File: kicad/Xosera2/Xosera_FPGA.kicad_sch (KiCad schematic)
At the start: 99 parts, among them J1 47589-0001, U1 93LC56BT-I/OT, U2 ICE40UP5K-SG48ITR, U3 FT232H, U4 SG-210STF 12.0000ML3, U5 W25Q32JVSSIM, U6 AP2127K-3.3, U7 AP2127K-1.2, U8 SN74AUP2G125DCUR

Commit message: Make a start on placement
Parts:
- removed H1, H2, H3, H4: MountingHole, vs:MountingHole_2.5mm_M3, symbol UPduino_v3.0:Mechanical_MountingHole
- J1: footprint vs:USB_Micro_AB_Female_0475890001 -> Connector_USB:USB_Micro-AB_Molex_47590-0001
- SJ19, SJ24, SJ25, SJ26: footprint vs:SolderJumper-2_0603_Open_TrianglePad1.0x1.5mm -> Jumper:SolderJumper-2_P1.3mm_Open_RoundedPad1.0x1.5mm
- SJ20, SJ31, SJ34, SJ35, SJ36: footprint vs:ShortedJumper-2_P1.3mm_Bridged_Pad1.0x1.0mm -> Jumper:SolderJumper-2_P1.3mm_Bridged2Bar_RoundedPad1.0x1.5mm
- U1: footprint vs:SOT-23-6 -> Package_TO_SOT_SMD:SOT-23-6
- U3: footprint vs:QFN-48-1EP_8x8mm_P0.5mm_EP6.2x6.2mm -> Package_DFN_QFN:QFN-48-1EP_8x8mm_P0.5mm_EP6.2x6.2mm
- U4: footprint vs:Oscillator_SMD_Abracon_ASDMB-4Pin_2.5x2.0mm -> Oscillator:Oscillator_SMD_Abracon_ASDMB-4Pin_2.5x2.0mm
- U6, U7: footprint vs:SOT-23-5 -> Package_TO_SOT_SMD:SOT-23-5

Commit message: Replace all GALs with one 1504
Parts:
- C10, C12, C13, C14, C15, C16, C18, C2, C25, C3, C36, C4, C5, C6, C7, C8, C9: value 0.1u -> 100n; footprint Capacitor_SMD:C_0603_1608Metric -> Capacitor_SMD:C_0402_1005Metric
- C17: value 0.1u -> 100m; footprint Capacitor_SMD:C_0603_1608Metric -> Capacitor_SMD:C_0402_1005Metric
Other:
- title: Xosera rosco_m68k daughterboard -> rosco_m68k Super Board
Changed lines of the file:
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@@
   (paper "A3")
   (title_block
-    (title "Xosera rosco_m68k daughterboard")
-    (date "2024-02-08")
+    (title "rosco_m68k Super Board")
+    (date "2024-02-11")
     (rev "0")
     (company "The Really Old-School Company Limited & XarkLabs")
     (comment 1 "Copyright (c)2023")
     (comment 2 "CERN OHL & MIT License")
+    (comment 3 "Featuring Xosera & MarkM's IDE")
   )
   (junction (at 262.89 208.28) (diameter 0) (color 0 0 0 0)
@@
       (effects (font (size 1.27 1.27)) (justify left))
     )
-    (property "Value" "0.1u" (at 141.351 181.483 0)
+    (property "Value" "100n" (at 141.351 181.483 0)
       (effects (font (size 1.27 1.27)) (justify left))
     )
-    (property "Footprint" "Capacitor_SMD:C_0603_1608Metric" (at 139.3952 184.15 0)
+    (property "Footprint" "Capacitor_SMD:C_0402_1005Metric" (at 139.3952 184.15 0)
       (effects (font (size 1.27 1.27)) hide)
     )
@@
       (effects (font (size 1.27 1.27)) (justify left))
     )
-    (property "Value" "0.1u" (at 121.031 181.483 0)
+    (property "Value" "100n" (at 121.031 181.483 0)
       (effects (font (size 1.27 1.27)) (justify left))
     )
-    (property "Footprint" "Capacitor_SMD:C_0603_1608Metric" (at 119.0752 184.15 0)
+    (property "Footprint" "Capacitor_SMD:C_0402_1005Metric" (at 119.0752 184.15 0)
       (effects (font (size 1.27 1.27)) hide)
     )
@@
       (effects (font (size 1.27 1.27)) (justify left))
     )
-    (property "Value" "0.1u" (at 43.561 195.453 0)
+    (property "Value" "100n" (at 43.561 195.453 0)
       (effects (font (size 1.27 1.27)) (justify left))
     )
-    (property "Footprint" "Capacitor_SMD:C_0603_1608Metric" (at 41.6052 198.12 0)
+    (property "Footprint" "Capacitor_SMD:C_0402_1005Metric" (at 41.6052 198.12 0)
       (effects (font (size 1.27 1.27)) hide)
     )
@@
       (effects (font (size 1.27 1.27)) (justify left))
     )
-    (property "Value" "0.1u" (at 61.341 181.483 0)
+    (property "Value" "100n" (at 61.341 181.483 0)
       (effects (font (size 1.27 1.27)) (justify left))
     )
-    (property "Footprint" "Capacitor_SMD:C_0603_1608Metric" (at 59.3852 184.15 0)
+    (property "Footprint" "Capacitor_SMD:C_0402_1005Metric" (at 59.3852 184.15 0)
       (effects (font (size 1.27 1.27)) hide)
     )
@@
       (effects (font (size 1.27 1.27)) (justify left))
     )
-    (property "Value" "0.1u" (at 62.611 104.013 0)
+    (property "Value" "100n" (at 62.611 104.013 0)
       (effects (font (size 1.27 1.27)) (justify left))
     )
-    (property "Footprint" "Capacitor_SMD:C_0603_1608Metric" (at 60.6552 106.68 0)
+    (property "Footprint" "Capacitor_SMD:C_0402_1005Metric" (at 60.6552 106.68 0)
       (effects (font (size 1.27 1.27)) hide)
     )
@@
       (effects (font (size 1.27 1.27)) (justify left))
     )
-    (property "Value" "0.1u" (at 53.721 50.673 0)
+    (property "Value" "100n" (at 53.721 50.673 0)
       (effects (font (size 1.27 1.27)) (justify left))
     )
-    (property "Footprint" "Capacitor_SMD:C_0603_1608Metric" (at 51.7652 53.34 0)
+    (property "Footprint" "Capacitor_SMD:C_0402_1005Metric" (at 51.7652 53.34 0)
       (effects (font (size 1.27 1.27)) hide)
     )
@@
       (effects (font (size 1.27 1.27)) (justify left))
     )
-    (property "Value" "0.1u" (at 376.301 74.803 0)
+    (property "Value" "100n" (at 376.301 74.803 0)
       (effects (font (size 1.27 1.27)) (justify left))
     )
-    (property "Footprint" "Capacitor_SMD:C_0603_1608Metric" (at 374.3452 77.47 0)
+    (property "Footprint" "Capacitor_SMD:C_0402_1005Metric" (at 374.3452 77.47 0)
       (effects (font (size 1.27 1.27)) hide)
     )
@@
       (effects (font (size 1.27 1.27)))
     )
-    (property "Value" "0.1u" (at 74.93 207.01 90)
+    (property "Value" "100n" (at 74.93 207.01 90)
       (effects (font (size 1.27 1.27)))
     )
-    (property "Footprint" "Capacitor_SMD:C_0603_1608Metric" (at 71.12 203.2 0)
+    (property "Footprint" "Capacitor_SMD:C_0402_1005Metric" (at 71.12 203.2 0)
       (effects (font (size 1.27 1.27)) hide)
     )
@@
       (effects (font (size 1.27 1.27)) (justify left))
     )
-    (property "Value" "0.1u" (at 165.481 172.593 0)
+    (property "Value" "100n" (at 165.481 172.593 0)
       (effects (font (size 1.27 1.27)) (justify left))
     )
-    (property "Footprint" "Capacitor_SMD:C_0603_1608Metric" (at 163.5252 175.26 0)
+    (property "Footprint" "Capacitor_SMD:C_0402_1005Metric" (at 163.5252 175.26 0)
       (effects (font (size 1.27 1.27)) hide)
     )
@@
       (effects (font (size 1.27 1.27)) (justify left))
     )
-    (property "Value" "0.1u" (at 215.011 82.423 0)
+    (property "Value" "100n" (at 215.011 82.423 0)
       (effects (font (size 1.27 1.27)) (justify left))
     )
-    (property "Footprint" "Capacitor_SMD:C_0603_1608Metric" (at 213.0552 85.09 0)
+    (property "Footprint" "Capacitor_SMD:C_0402_1005Metric" (at 213.0552 85.09 0)
       (effects (font (size 1.27 1.27)) hide)
     )
@@
       (effects (font (size 1.27 1.27)) (justify left))
     )
-    (property "Value" "0.1u" (at 131.191 181.483 0)
+    (property "Value" "100n" (at 131.191 181.483 0)
       (effects (font (size 1.27 1.27)) (justify left))
     )
-    (property "Footprint" "Capacitor_SMD:C_0603_1608Metric" (at 129.2352 184.15 0)
+    (property "Footprint" "Capacitor_SMD:C_0402_1005Metric" (at 129.2352 184.15 0)
       (effects (font (size 1.27 1.27)) hide)
     )
@@
       (effects (font (size 1.27 1.27)) (justify left))
     )
-    (property "Value" "0.1u" (at 310.261 39.243 0)
+    (property "Value" "100n" (at 310.261 39.243 0)
       (effects (font (size 1.27 1.27)) (justify left))
     )
-    (property "Footprint" "Capacitor_SMD:C_0603_1608Metric" (at 308.3052 41.91 0)
+    (property "Footprint" "Capacitor_SMD:C_0402_1005Metric" (at 308.3052 41.91 0)
       (effects (font (size 1.27 1.27)) hide)
     )
@@
       (effects (font (size 1.27 1.27)) (justify left))
     )
-    (property "Value" "0.1u" (at 281.051 83.693 0)
+    (property "Value" "100n" (at 281.051 83.693 0)
       (effects (font (size 1.27 1.27)) (justify left))
     )
-    (property "Footprint" "Capacitor_SMD:C_0603_1608Metric" (at 279.0952 86.36 0)
+    (property "Footprint" "Capacitor_SMD:C_0402_1005Metric" (at 279.0952 86.36 0)
       (effects (font (size 1.27 1.27)) hide)
     )
@@
       (effects (font (size 1.27 1.27)) (justify left))
     )
-    (property "Value" "0.1u" (at 27.051 267.843 0)
+    (property "Value" "100n" (at 27.051 267.843 0)
       (effects (font (size 1.27 1.27)) (justify left))
     )
-    (property "Footprint" "Capacitor_SMD:C_0603_1608Metric" (at 25.0952 270.51 0)
+    (property "Footprint" "Capacitor_SMD:C_0402_1005Metric" (at 25.0952 270.51 0)
       (effects (font (size 1.27 1.27)) hide)
     )
@@
       (effects (font (size 1.27 1.27)) (justify left))
     )
-    (property "Value" "0.1u" (at 164.211 83.693 0)
+    (property "Value" "100n" (at 164.211 83.693 0)
       (effects (font (size 1.27 1.27)) (justify left))
     )
-    (property "Footprint" "Capacitor_SMD:C_0603_1608Metric" (at 162.2552 86.36 0)
+    (property "Footprint" "Capacitor_SMD:C_0402_1005Metric" (at 162.2552 86.36 0)
       (effects (font (size 1.27 1.27)) hide)
     )
@@
       (effects (font (size 1.27 1.27)) (justify left))
     )
-    (property "Value" "0.1u" (at 197.231 197.993 0)
+    (property "Value" "100m" (at 197.231 197.993 0)
       (effects (font (size 1.27 1.27)) (justify left))
     )
-    (property "Footprint" "Capacitor_SMD:C_0603_1608Metric" (at 195.2752 200.66 0)
+    (property "Footprint" "Capacitor_SMD:C_0402_1005Metric" (at 195.2752 200.66 0)
       (effects (font (size 1.27 1.27)) hide)
     )
@@
       (effects (font (size 1.27 1.27)) (justify left))
     )
-    (property "Value" "0.1u" (at 165.481 186.563 0)
+    (property "Value" "100n" (at 165.481 186.563 0)
       (effects (font (size 1.27 1.27)) (justify left))
     )
-    (property "Footprint" "Capacitor_SMD:C_0603_1608Metric" (at 163.5252 189.23 0)
+    (property "Footprint" "Capacitor_SMD:C_0402_1005Metric" (at 163.5252 189.23 0)
       (effects (font (size 1.27 1.27)) hide)
     )
@@
       (effects (font (size 1.27 1.27)) (justify left))
     )
-    (property "Value" "0.1u" (at 44.831 104.013 0)
+    (property "Value" "100n" (at 44.831 104.013 0)
       (effects (font (size 1.27 1.27)) (justify left))
     )
-    (property "Footprint" "Capacitor_SMD:C_0603_1608Metric" (at 42.8752 106.68 0)
+    (property "Footprint" "Capacitor_SMD:C_0402_1005Metric" (at 42.8752 106.68 0)
       (effects (font (size 1.27 1.27)) hide)
     )

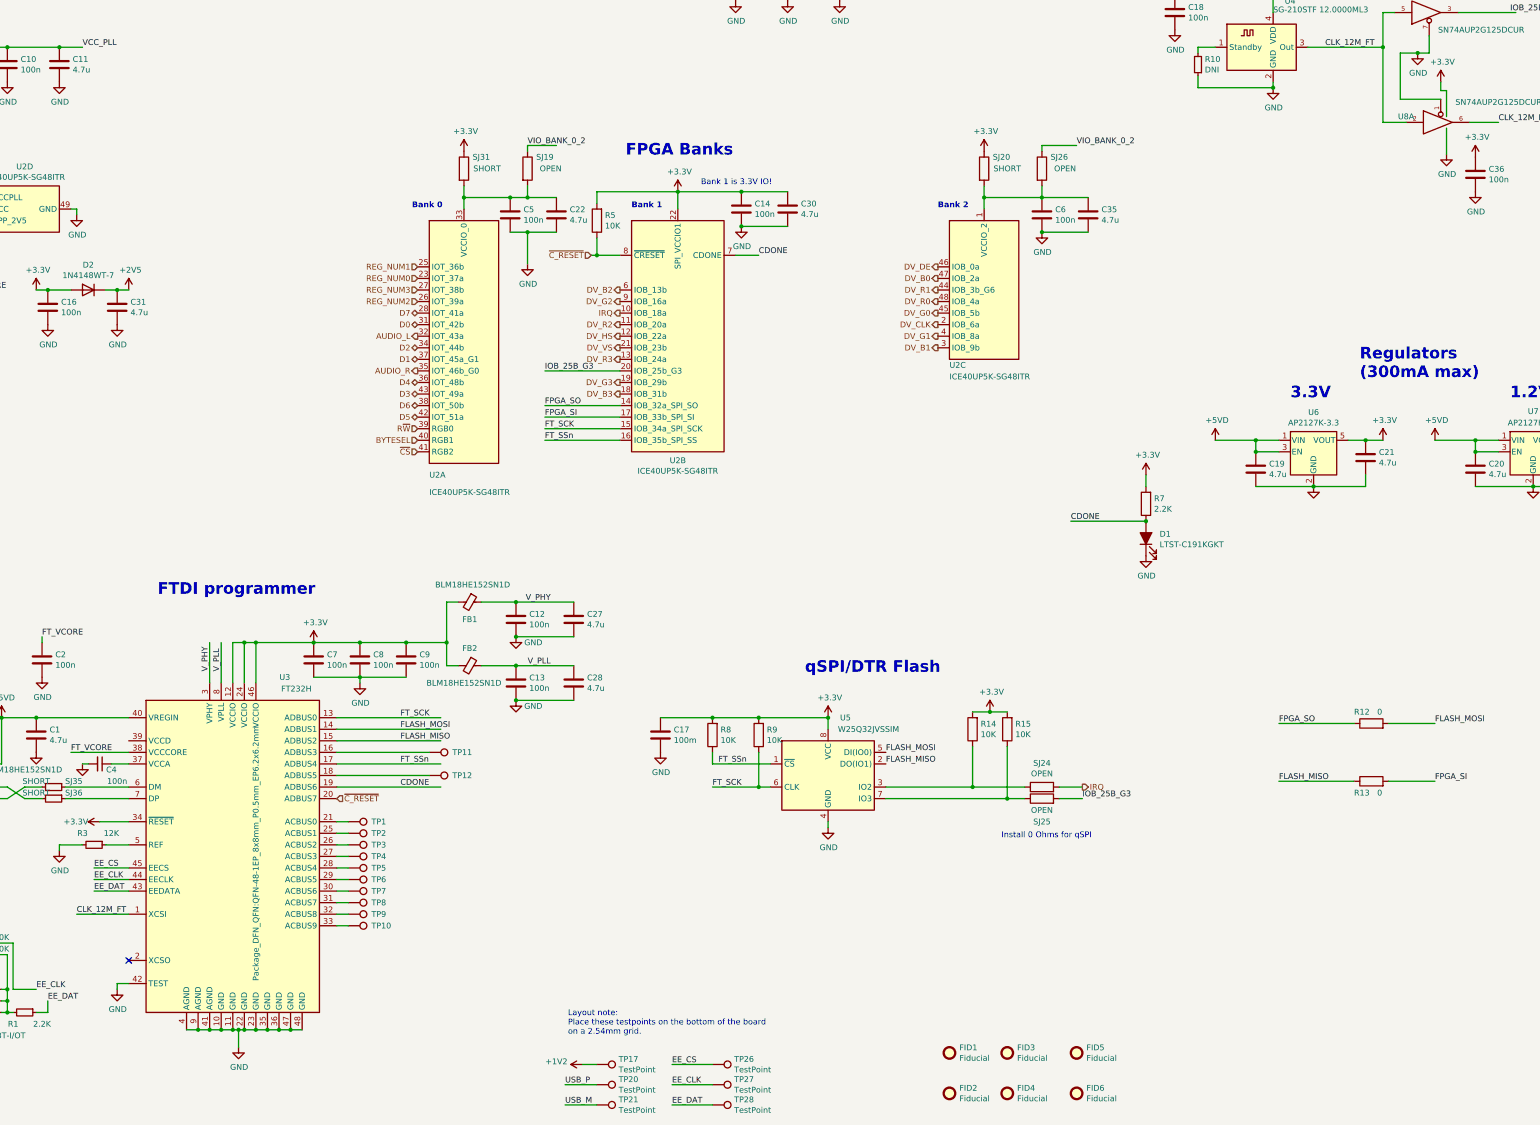
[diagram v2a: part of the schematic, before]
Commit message: Fix ERC (mostly) and sort out footprints etc
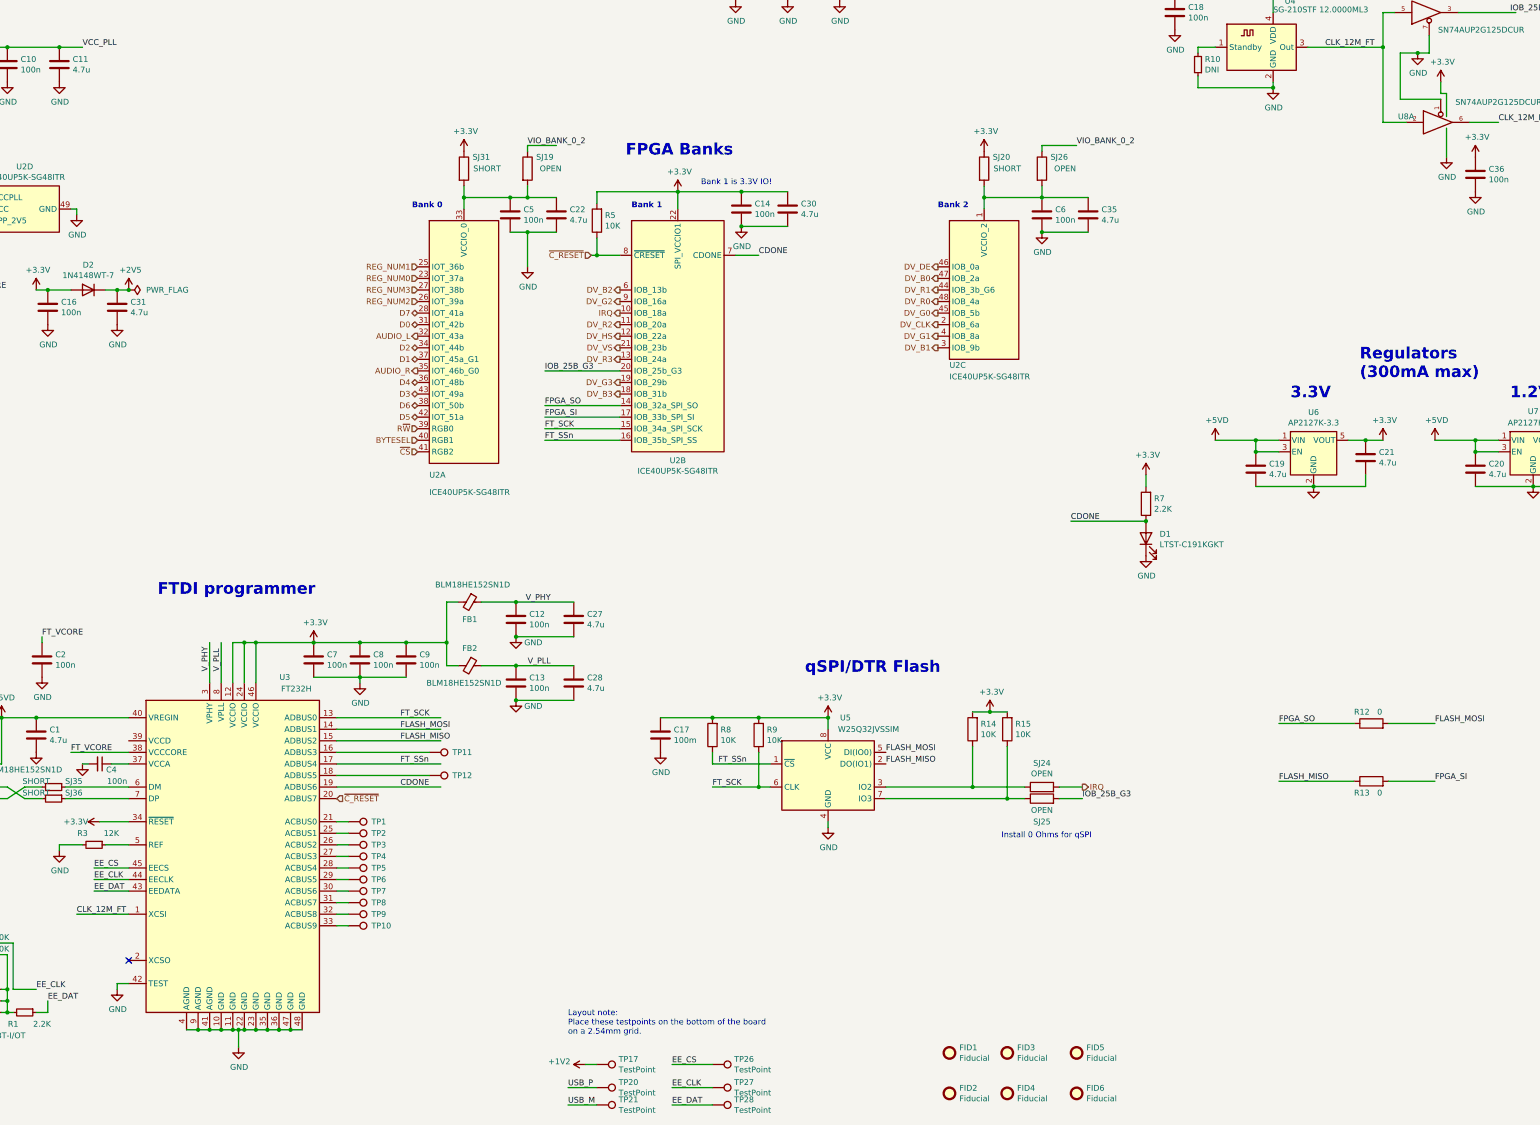
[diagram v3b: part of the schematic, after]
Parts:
- D1: symbol UPduino_v3.0:Device_LED_ALT -> Device:LED
- D2: symbol UPduino_v3.0:Diode_1N4148W -> Diode:1N4148W
- FB1, FB2, FB3: symbol UPduino_v3.0:Device_Ferrite_Bead_Small -> Device:FerriteBead_Small
- FID1, FID2, FID3, FID4, FID5, FID6: symbol UPduino_v3.0:Fiducial-Mechanical -> Mechanical:Fiducial
- J1: symbol UPduino_v3.0:Connector_USB_B_Micro -> Connector:USB_B_Micro
- TP1, TP10, TP11, TP12, TP17, TP2, TP20, TP21, TP26, TP27, TP28, TP3, TP4, TP5, TP6, TP7, TP8, TP9: symbol UPduino_v3.0:Connector_TestPoint -> Connector:TestPoint
- U1: symbol UPduino_v3.0:93LCxxBxxOT-Memory_EEPROM -> UPduino Imports:93LCxxBxxOT-Memory_EEPROM
- U2: symbol UPduino_v3.0:ICE40UP5K-SG48ITR-FPGA_Lattice -> UPduino Imports:ICE40UP5K-SG48ITR-FPGA_Lattice
- U3: symbol UPduino_v3.0:Interface_USB_FT232H -> Interface_USB:FT232H
- U4: symbol UPduino_v3.0:ASDMB-xxxMHz-Oscillator -> Oscillator:ASDMB-xxxMHz
- U5: symbol UPduino_v3.0:W25Q32JVSS-Memory_Flash -> UPduino Imports:W25Q32JVSS-Memory_Flash
- U6: symbol UPduino_v3.0:AP2127K-3.3 -> Regulator_Linear:AP2127K-3.3
- U7: symbol UPduino_v3.0:AP2127K-1.2 -> Regulator_Linear:AP2127K-1.2
- U8: footprint (none) -> Package_SO:VSSOP-8_2.3x2mm_P0.5mm; symbol UPduino_v3.0:74xGxx_74AUC2G125 -> UPduino Imports:74xGxx_74AUC2G125
- U8: symbol UPduino_v3.0:74xGxx_74AUC2G125 -> UPduino Imports:74xGxx_74AUC2G125
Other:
- moved on the sheet: TP20, TP27

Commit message: Fix Kicad weirdness
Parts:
- removed J1: 47589-0001, Connector_USB:USB_Micro-AB_Molex_47590-0001, symbol Connector:USB_B_Micro
- removed SJ35, SJ36: SHORT, Jumper:SolderJumper-2_P1.3mm_Bridged2Bar_RoundedPad1.0x1.5mm, symbol Device:R_Small
- added J1: USB_C, Connector_USB:USB_C_Receptacle_Palconn_UTC16-G, symbol Connector:USB_C_Receptacle_USB2.0
- added R2 (x2): 5.1K, Resistor_SMD:R_0805_2012Metric_Pad1.20x1.40mm_HandSolder, symbol Device:R
- added R2, R3: 22R, Resistor_SMD:R_0805_2012Metric_Pad1.20x1.40mm_HandSolder, symbol Device:R
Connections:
- net EE_CLK: now also U1.4 (CLK)
- net EE_DAT: now also U1.3 (DI)
- net GND: now also J1.A1 (GND), J1.A12 (GND), J1.B1 (GND), J1.B12 (GND), J1.S1 (SHIELD), R2.2, R2.2
- net USB_M: now also J1.A7 (D-), J1.B7 (D-), R2.2
- net USB_P: now also J1.A6 (D+), J1.B6 (D+), R3.2
- net V_USB: now also J1.A4 (VBUS), J1.A9 (VBUS), J1.B4 (VBUS), J1.B9 (VBUS)
- net at U3.6 (DM): now also R2.1
- net at U3.7 (DP): now also R3.1
- net at R1.2, R4.1, U1.1 (DO): no longer U1.3 (DI), U1.4 (CLK)
- new net: J1.A5 (CC1), R2.1
- new net: J1.B5 (CC2), R2.1
- no-connect marks 2 -> 3
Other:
- moved on the sheet: C1, C12, C13, C17, C2, C25, C27, C28, C3, C4, C7, C8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

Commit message: Initial layout, delete some useless things
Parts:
- removed FID1, FID2, FID3, FID4, FID5, FID6: Fiducial, Fiducial:Fiducial_0.75mm_Mask1.5mm, symbol Mechanical:Fiducial
- removed TP1, TP10, TP11, TP12, TP17, TP2, TP20, TP21, TP26, TP27, TP28, TP3, TP4, TP5, TP6, TP7, TP8, TP9: TestPoint, TestPoint:TestPoint_Pad_D1.0mm, symbol Connector:TestPoint
- added SJ24: OPEN, Jumper:SolderJumper-2_P1.3mm_Open_RoundedPad1.0x1.5mm, symbol Device:R
- added SJ24: SHORT, Jumper:SolderJumper-2_P1.3mm_Bridged_RoundedPad1.0x1.5mm, symbol Device:R
- added U10: TPS22929D, Package_TO_SOT_SMD:SOT-23-6, symbol Power_Management:TPS22929D
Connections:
- net +5V: now also SJ24.2, U10.1 (VOUT); no longer C1.1, FB3.1, U3.40 (VREGIN)
- net GND: now also U10.2 (GND), U10.5 (GND)
- net +3.3V renamed +3V3
- net USB_M renamed USB_N
- new net: C1.1, FB3.1, SJ24.1, SJ24.1, U10.4 (VIN), U10.6 (VIN), U3.40 (VREGIN)
- new net: SJ24.2, U10.3 (ON)
- no-connect marks 3 -> 15
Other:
- note removed: "Layout note: Place these testpoints on the bottom of the board on a 2.54mm grid."
- moved on the sheet: C2
